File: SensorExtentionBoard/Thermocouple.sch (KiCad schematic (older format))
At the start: 9 parts, among them J8 Conn_01x02_Male, J9 Conn_01x02_Male, U4 MCP4728, U5 TS3A24159DGSR, U6 TS3A24159DGSR

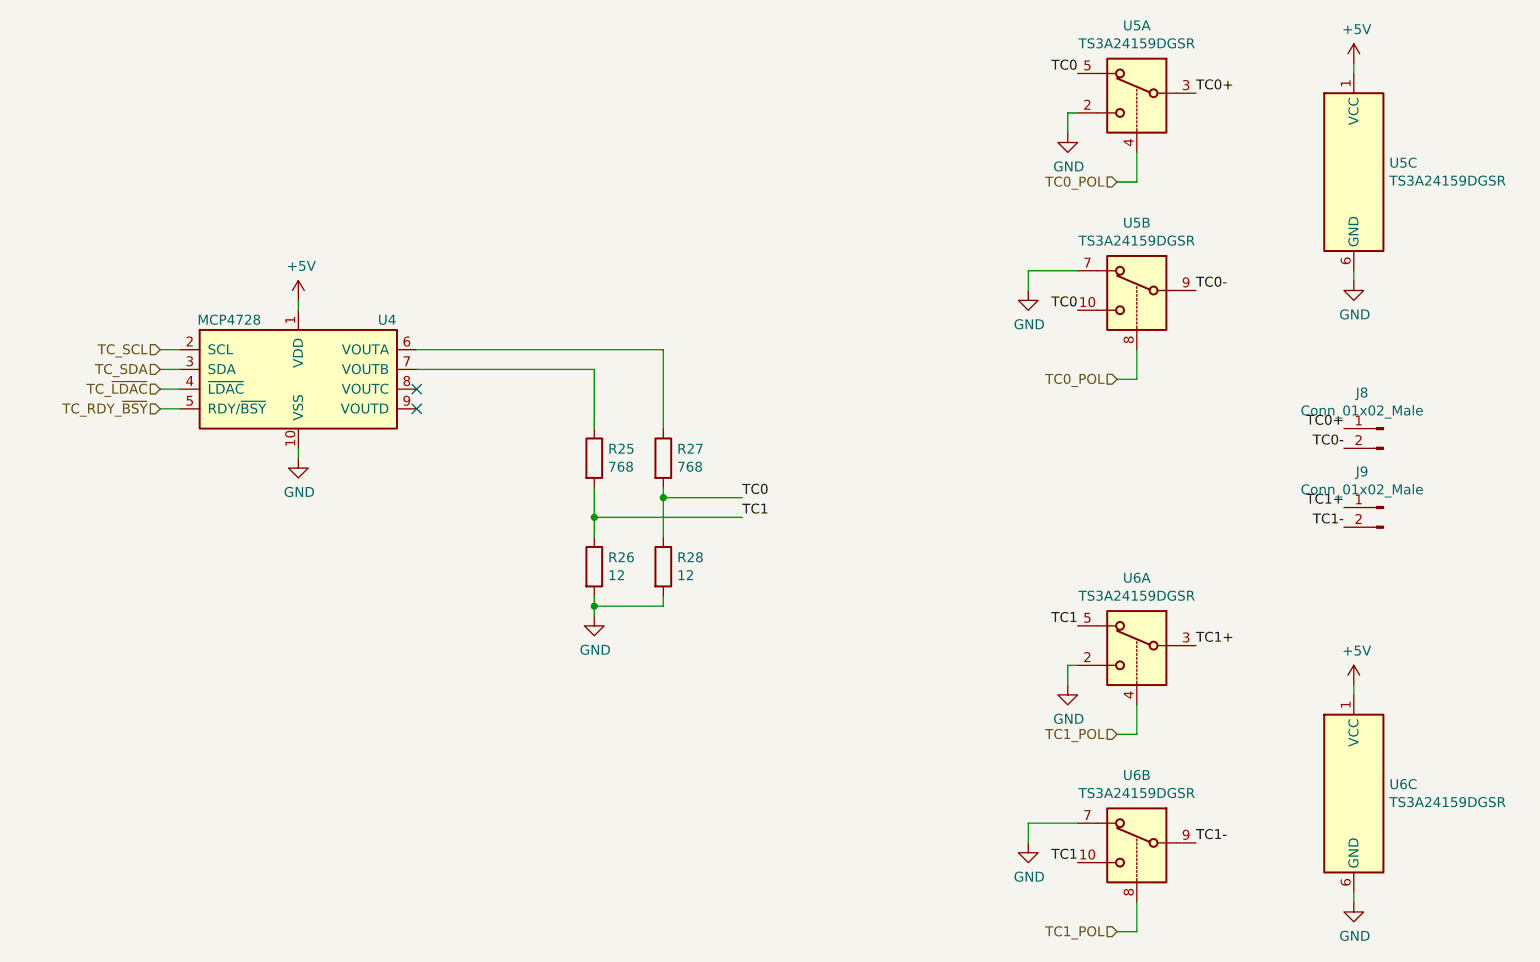
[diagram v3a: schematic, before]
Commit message: Replaced ADS1115 with ADS1015 on PT page
The ADS1115 is being used to read the voltages provided by the Helix
system to the pressure transducers. The ADS1015 is already doing
the same job for the Hall Effect sensors, however the ADS1015 has
4 bits lower accuracy. High accuracy is not needed for this
application so be replacing the ADS1115 with the ADS1015 we can
reduce cost and more importantly reduce BOM size making the project
logistics easier to manage.
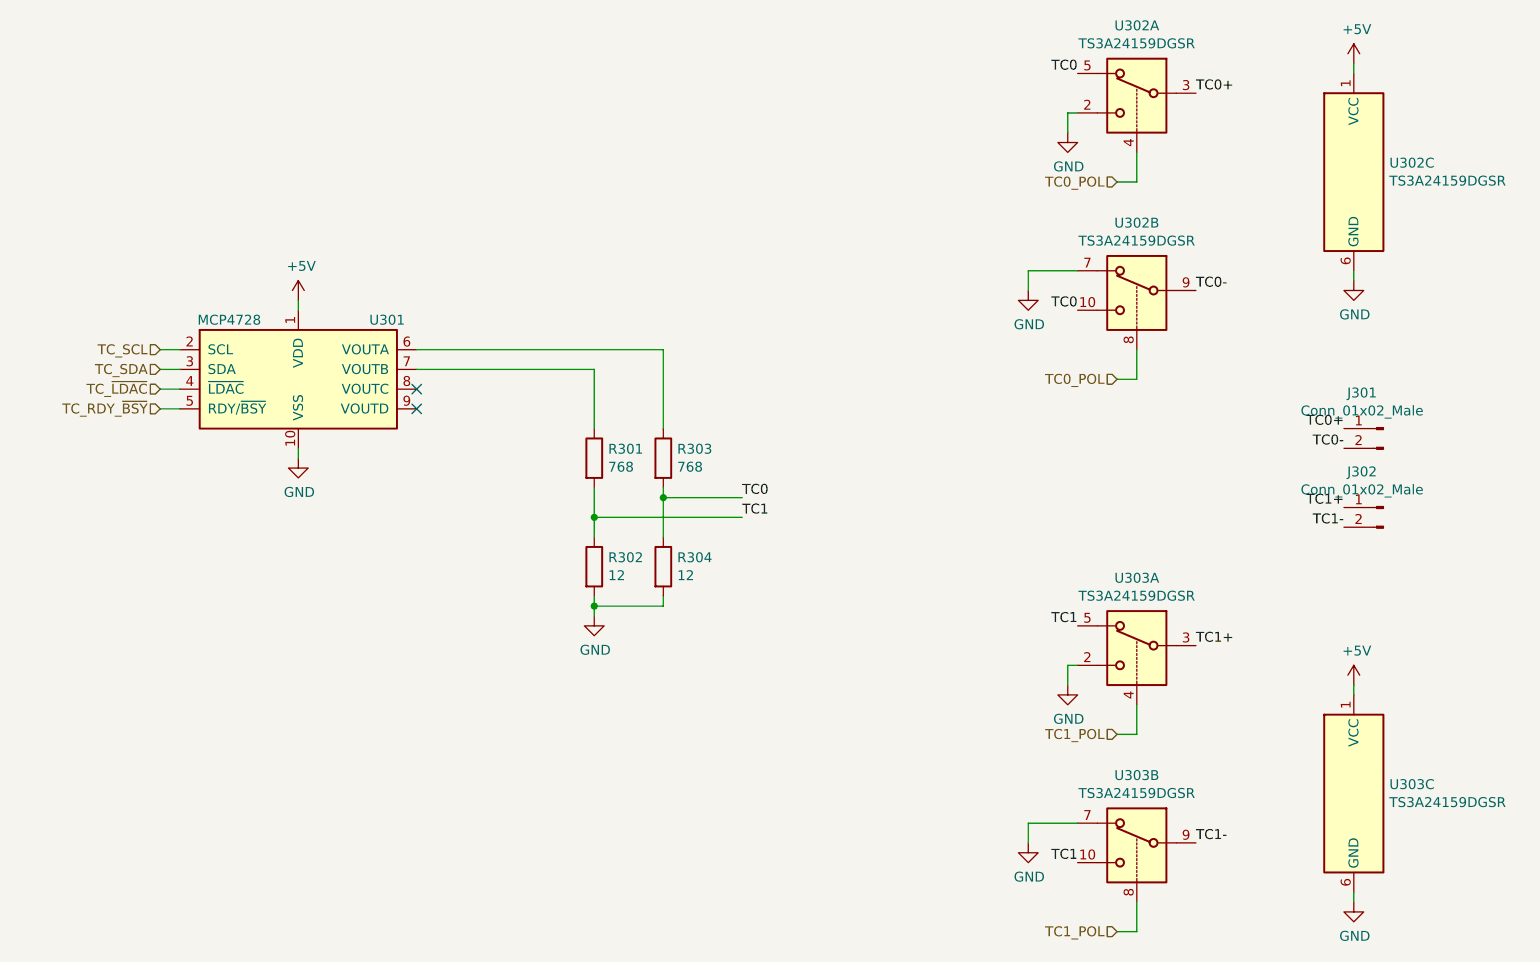
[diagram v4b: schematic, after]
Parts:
- renumbered J8 to J301, J9 to J302, R25 to R301, R26 to R302, R27 to R303, R28 to R304, U4 to U301, U5 to U302, U6 to U303
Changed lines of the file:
@@
 $EndDescr
 $Comp
-L Analog_DAC:MCP4728 U4
+L Analog_DAC:MCP4728 U301
 U 1 1 5E2FD865
 P 4000 2350
-F 0 "U4" H 4450 2600 50  0000 C CNN
+F 0 "U301" H 4450 2600 50  0000 C CNN
 F 1 "MCP4728" H 3650 2600 50  0000 C CNN
 F 2 "Package_SO:MSOP-10_3x3mm_P0.5mm" H 4000 1750 50  0001 C CNN
@@
 $EndComp
 $Comp
-L power:GND #PWR025
+L power:GND #PWR0302
 U 1 1 5E2FE6B0
 P 4000 2800
-F 0 "#PWR025" H 4000 2550 50  0001 C CNN
+F 0 "#PWR0302" H 4000 2550 50  0001 C CNN
 F 1 "GND" H 4005 2627 50  0000 C CNN
 F 2 "" H 4000 2800 50  0001 C CNN
@@
 	4000 2800 4000 2750
 $Comp
-L power:+5V #PWR024
+L power:+5V #PWR0301
 U 1 1 5E2FE9D8
 P 4000 2000
-F 0 "#PWR024" H 4000 1850 50  0001 C CNN
+F 0 "#PWR0301" H 4000 1850 50  0001 C CNN
 F 1 "+5V" H 4015 2173 50  0000 C CNN
 F 2 "" H 4000 2000 50  0001 C CNN
@@
 	3300 2450 3400 2450
 $Comp
-L Device:R R27
+L Device:R R303
 U 1 1 5E3006EF
 P 5850 2800
-F 0 "R27" H 5920 2846 50  0000 L CNN
+F 0 "R303" H 5920 2846 50  0000 L CNN
 F 1 "768" H 5920 2755 50  0000 L CNN
 F 2 "Resistor_SMD:R_1206_3216Metric_Pad1.42x1.75mm_HandSolder" V 5780 2800 50  0001 C CNN
@@
 $EndComp
 $Comp
-L Device:R R28
+L Device:R R304
 U 1 1 5E300948
 P 5850 3350
-F 0 "R28" H 5920 3396 50  0000 L CNN
+F 0 "R304" H 5920 3396 50  0000 L CNN
 F 1 "12" H 5920 3305 50  0000 L CNN
 F 2 "Resistor_SMD:R_1206_3216Metric_Pad1.42x1.75mm_HandSolder" V 5780 3350 50  0001 C CNN
@@
 $EndComp
 $Comp
-L Device:R R25
+L Device:R R301
 U 1 1 5E3082B4
 P 5500 2800
-F 0 "R25" H 5570 2846 50  0000 L CNN
+F 0 "R301" H 5570 2846 50  0000 L CNN
 F 1 "768" H 5570 2755 50  0000 L CNN
 F 2 "Resistor_SMD:R_1206_3216Metric_Pad1.42x1.75mm_HandSolder" V 5430 2800 50  0001 C CNN
@@
 $EndComp
 $Comp
-L Device:R R26
+L Device:R R302
 U 1 1 5E3082BA
 P 5500 3350
-F 0 "R26" H 5570 3396 50  0000 L CNN
+F 0 "R302" H 5570 3396 50  0000 L CNN
 F 1 "12" H 5570 3305 50  0000 L CNN
 F 2 "Resistor_SMD:R_1206_3216Metric_Pad1.42x1.75mm_HandSolder" V 5430 3350 50  0001 C CNN
@@
 	5500 3100 5500 3200
 $Comp
-L power:GND #PWR026
+L power:GND #PWR0303
 U 1 1 5E3159B6
 P 5500 3600
-F 0 "#PWR026" H 5500 3350 50  0001 C CNN
+F 0 "#PWR0303" H 5500 3350 50  0001 C CNN
 F 1 "GND" H 5505 3427 50  0000 C CNN
 F 2 "" H 5500 3600 50  0001 C CNN
@@
 NoConn ~ 4600 2450
 $Comp
-L Analog_Switch:TS3A24159DGSR U5
+L Analog_Switch:TS3A24159DGSR U302
 U 3 1 5E318CFB
 P 9350 1350
-F 0 "U5" H 9530 1396 50  0000 L CNN
+F 0 "U302" H 9530 1396 50  0000 L CNN
 F 1 "TS3A24159DGSR" H 9530 1305 50  0000 L CNN
 F 2 "Package_SO:TSSOP-10_3x3mm_P0.5mm" H 9350 1000 50  0001 C CNN
@@
 $EndComp
 $Comp
-L power:+5V #PWR031
+L power:+5V #PWR0308
 U 1 1 5E33134D
 P 9350 800
-F 0 "#PWR031" H 9350 650 50  0001 C CNN
+F 0 "#PWR0308" H 9350 650 50  0001 C CNN
 F 1 "+5V" H 9365 973 50  0000 C CNN
 F 2 "" H 9350 800 50  0001 C CNN
@@
 	9350 800  9350 850
 $Comp
-L power:GND #PWR032
+L power:GND #PWR0309
 U 1 1 5E332A5C
 P 9350 1900
-F 0 "#PWR032" H 9350 1650 50  0001 C CNN
+F 0 "#PWR0309" H 9350 1650 50  0001 C CNN
 F 1 "GND" H 9355 1727 50  0000 C CNN
 F 2 "" H 9350 1900 50  0001 C CNN
@@
 TC0
 $Comp
-L power:GND #PWR027
+L power:GND #PWR0304
 U 1 1 5E324555
 P 7700 1950
-F 0 "#PWR027" H 7700 1700 50  0001 C CNN
+F 0 "#PWR0304" H 7700 1700 50  0001 C CNN
 F 1 "GND" H 7705 1777 50  0000 C CNN
 F 2 "" H 7700 1950 50  0001 C CNN
@@
 $EndComp
 $Comp
-L power:GND #PWR029
+L power:GND #PWR0306
 U 1 1 5E324066
 P 7900 1150
-F 0 "#PWR029" H 7900 900 50  0001 C CNN
+F 0 "#PWR0306" H 7900 900 50  0001 C CNN
 F 1 "GND" H 7905 977 50  0000 C CNN
 F 2 "" H 7900 1150 50  0001 C CNN
@@
 TC0+
 $Comp
-L Analog_Switch:TS3A24159DGSR U5
+L Analog_Switch:TS3A24159DGSR U302
 U 2 1 5E317F40
 P 8250 1850
-F 0 "U5" H 8250 2092 50  0000 C CNN
+F 0 "U302" H 8250 2092 50  0000 C CNN
 F 1 "TS3A24159DGSR" H 8250 2001 50  0000 C CNN
 F 2 "Package_SO:TSSOP-10_3x3mm_P0.5mm" H 8250 1500 50  0001 C CNN
@@
 $EndComp
 $Comp
-L Analog_Switch:TS3A24159DGSR U5
+L Analog_Switch:TS3A24159DGSR U302
 U 1 1 5E31745F
 P 8250 850
-F 0 "U5" H 8250 1092 50  0000 C CNN
+F 0 "U302" H 8250 1092 50  0000 C CNN
 F 1 "TS3A24159DGSR" H 8250 1001 50  0000 C CNN
 F 2 "Package_SO:TSSOP-10_3x3mm_P0.5mm" H 8250 500 50  0001 C CNN
@@
 $EndComp
 $Comp
-L Analog_Switch:TS3A24159DGSR U6
+L Analog_Switch:TS3A24159DGSR U303
 U 3 1 5E35C1F5
 P 9350 4500
-F 0 "U6" H 9530 4546 50  0000 L CNN
+F 0 "U303" H 9530 4546 50  0000 L CNN
 F 1 "TS3A24159DGSR" H 9530 4455 50  0000 L CNN
 F 2 "Package_SO:TSSOP-10_3x3mm_P0.5mm" H 9350 4150 50  0001 C CNN
@@
 $EndComp
 $Comp
-L power:+5V #PWR033
+L power:+5V #PWR0310
 U 1 1 5E35C1FB
 P 9350 3950
-F 0 "#PWR033" H 9350 3800 50  0001 C CNN
+F 0 "#PWR0310" H 9350 3800 50  0001 C CNN
 F 1 "+5V" H 9365 4123 50  0000 C CNN
 F 2 "" H 9350 3950 50  0001 C CNN
@@
 	9350 3950 9350 4000
 $Comp
-L power:GND #PWR034
+L power:GND #PWR0311
 U 1 1 5E35C202
 P 9350 5050
-F 0 "#PWR034" H 9350 4800 50  0001 C CNN
+F 0 "#PWR0311" H 9350 4800 50  0001 C CNN
 F 1 "GND" H 9355 4877 50  0000 C CNN
 F 2 "" H 9350 5050 50  0001 C CNN
@@
 TC1
 $Comp
-L power:GND #PWR028
+L power:GND #PWR0305
 U 1 1 5E35C215
 P 7700 4750
-F 0 "#PWR028" H 7700 4500 50  0001 C CNN
+F 0 "#PWR0305" H 7700 4500 50  0001 C CNN
 F 1 "GND" H 7705 4577 50  0000 C CNN
 F 2 "" H 7700 4750 50  0001 C CNN
@@
 $EndComp
 $Comp
-L power:GND #PWR030
+L power:GND #PWR0307
 U 1 1 5E35C21B
 P 7900 3950
-F 0 "#PWR030" H 7900 3700 50  0001 C CNN
+F 0 "#PWR0307" H 7900 3700 50  0001 C CNN
 F 1 "GND" H 7905 3777 50  0000 C CNN
 F 2 "" H 7900 3950 50  0001 C CNN
@@
 TC1+
 $Comp
-L Analog_Switch:TS3A24159DGSR U6
+L Analog_Switch:TS3A24159DGSR U303
 U 2 1 5E35C223
 P 8250 4650
-F 0 "U6" H 8250 4892 50  0000 C CNN
+F 0 "U303" H 8250 4892 50  0000 C CNN
 F 1 "TS3A24159DGSR" H 8250 4801 50  0000 C CNN
 F 2 "Package_SO:TSSOP-10_3x3mm_P0.5mm" H 8250 4300 50  0001 C CNN
@@
 $EndComp
 $Comp
-L Analog_Switch:TS3A24159DGSR U6
+L Analog_Switch:TS3A24159DGSR U303
 U 1 1 5E35C229
 P 8250 3650
-F 0 "U6" H 8250 3892 50  0000 C CNN
+F 0 "U303" H 8250 3892 50  0000 C CNN
 F 1 "TS3A24159DGSR" H 8250 3801 50  0000 C CNN
 F 2 "Package_SO:TSSOP-10_3x3mm_P0.5mm" H 8250 3300 50  0001 C CNN
@@
 $EndComp
 $Comp
-L Connector:Conn_01x02_Male J8
+L Connector:Conn_01x02_Male J301
 U 1 1 5E388A81
 P 9500 2650
-F 0 "J8" H 9608 2831 50  0000 C CNN
+F 0 "J301" H 9608 2831 50  0000 C CNN
 F 1 "Conn_01x02_Male" H 9608 2740 50  0000 C CNN
 F 2 "Connector_Molex:Molex_MicroClasp_55932-0210_1x02_P2.00mm_Vertical" H 9500 2650 50  0001 C CNN
@@
 $EndComp
 $Comp
-L Connector:Conn_01x02_Male J9
+L Connector:Conn_01x02_Male J302
 U 1 1 5E391340
 P 9500 3050
-F 0 "J9" H 9608 3231 50  0000 C CNN
+F 0 "J302" H 9608 3231 50  0000 C CNN
 F 1 "Conn_01x02_Male" H 9608 3140 50  0000 C CNN
 F 2 "Connector_Molex:Molex_MicroClasp_55932-0210_1x02_P2.00mm_Vertical" H 9500 3050 50  0001 C CNN
